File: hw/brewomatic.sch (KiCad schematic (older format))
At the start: 32 parts, among them J1 CON_MAX31865, J10 TEST_MOC, J2 EXP1, J3 EXP2, J4 12V_IN, J5 230V_CONN, J6 HEATING_CONN, J7 PUMP_CONN, J8 12V_ALIM_CONN, J9 TEST_IN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

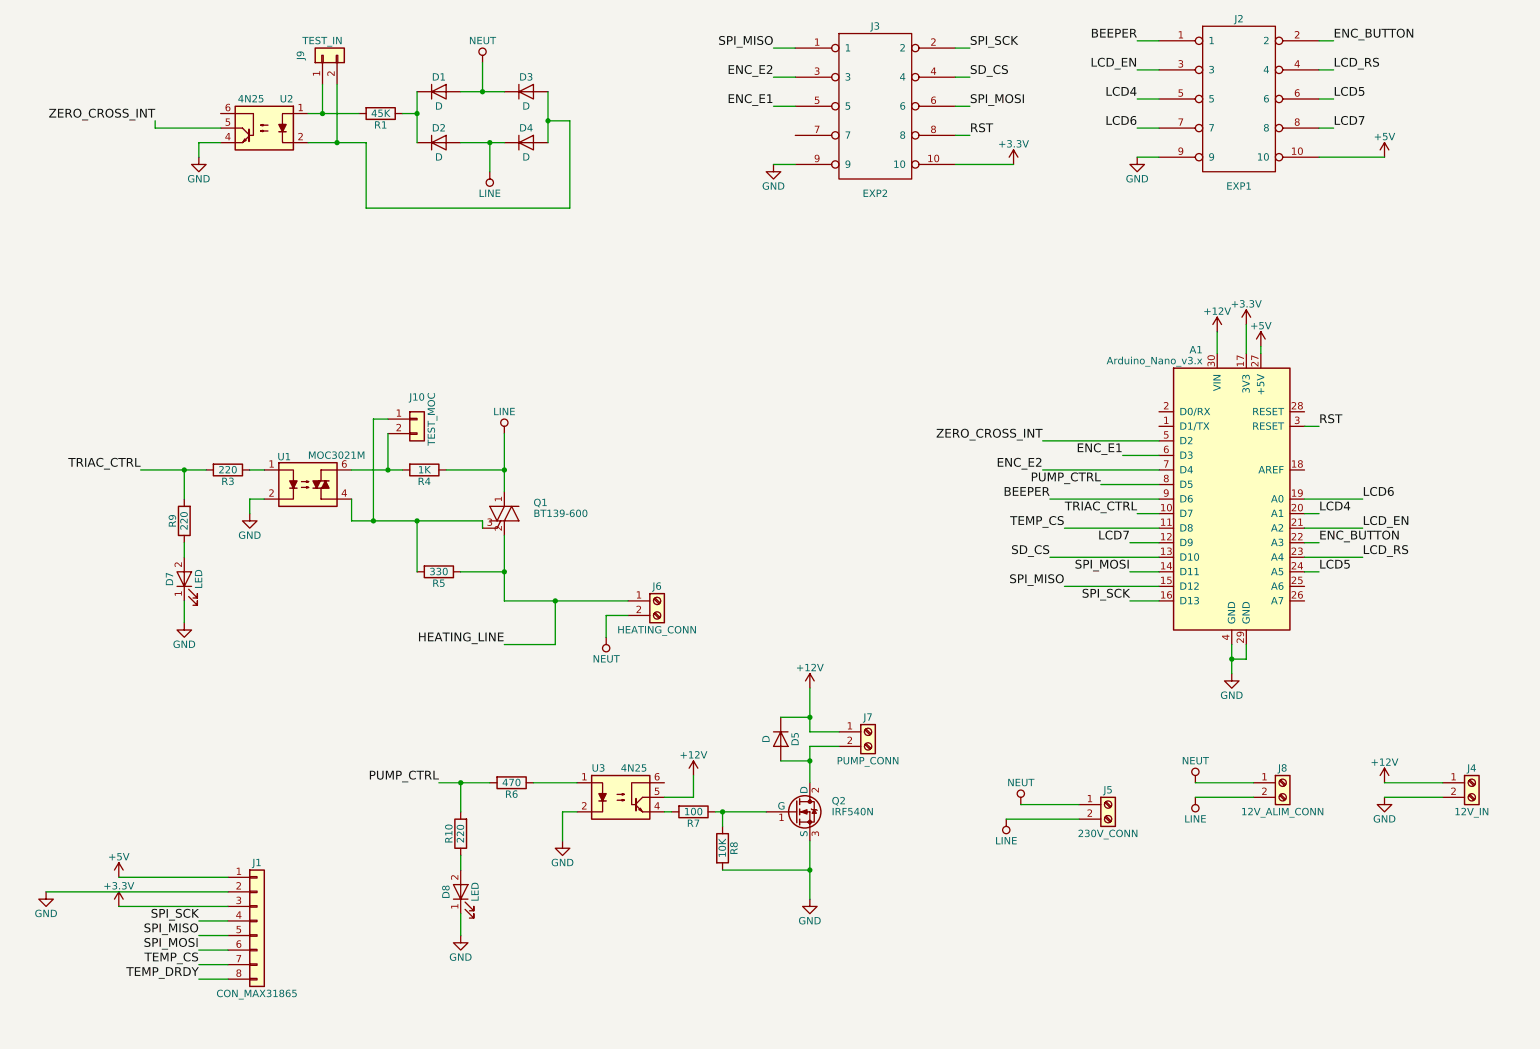
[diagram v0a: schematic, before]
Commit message: Reverse triac terminal since it only works in one direction and fix various problems
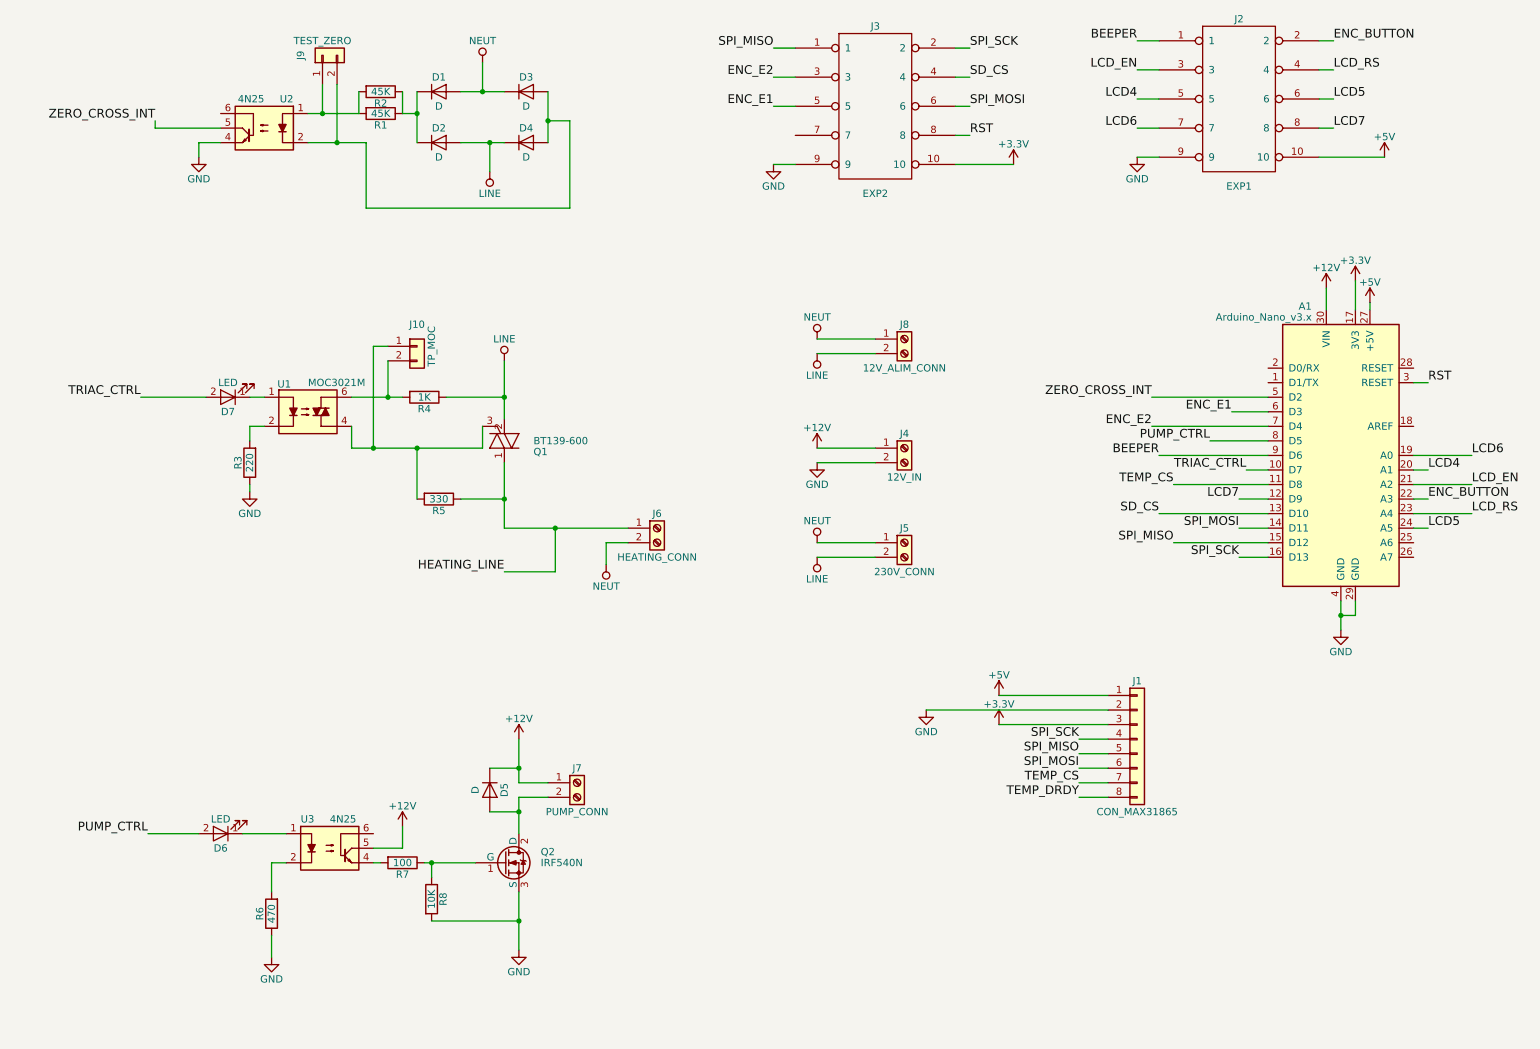
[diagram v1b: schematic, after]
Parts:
- removed D8: LED, LEDs:LED_D5.0mm, symbol LED
- removed R10, R9: 220, Resistors_SMD:R_0805_HandSoldering, symbol R
- added D6: LED, LEDs:LED_D5.0mm, symbol LED
- added R2: 45K, Resistors_THT:R_Axial_DIN0207_L6.3mm_D2.5mm_P10.16mm_Horizontal, symbol R
- J10: value TEST_MOC -> TP_MOC
- J9: value TEST_IN -> TEST_ZERO
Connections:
- net GND: now also R3.1, R6.1; no longer D7.1 (K), U1.2, U3.2
- net HEATING_LINE: now also Q1.1 (A1); no longer Q1.2 (A2)
- net LINE: now also Q1.2 (A2); no longer Q1.1 (A1)
- net PUMP_CTRL: now also D6.2 (A); no longer R6.2
- net TRIAC_CTRL: now also D7.2 (A); no longer R3.2
- net at J9.1 (Pin_1), R1.2, U2.1: now also R2.2
- net at U1.1: now also D7.1 (K); no longer R3.1
- net at D1.1 (K), D2.1 (K), R1.1: now also R2.1
- net at U3.1: now also D6.1 (K); no longer R6.1
- new net: R3.2, U1.2
- new net: R6.2, U3.2
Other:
- moved on the sheet: A1, D5, D7, J1, J10, J4, J5, J6, J7, J8, Q1, Q2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

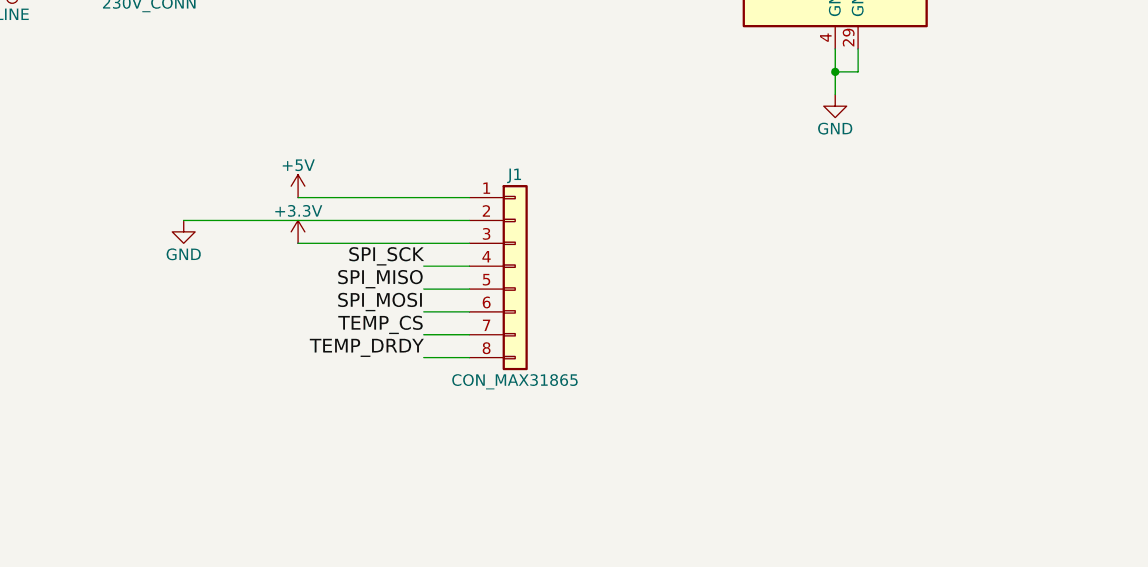
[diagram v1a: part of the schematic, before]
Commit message: Add 12V fan plug
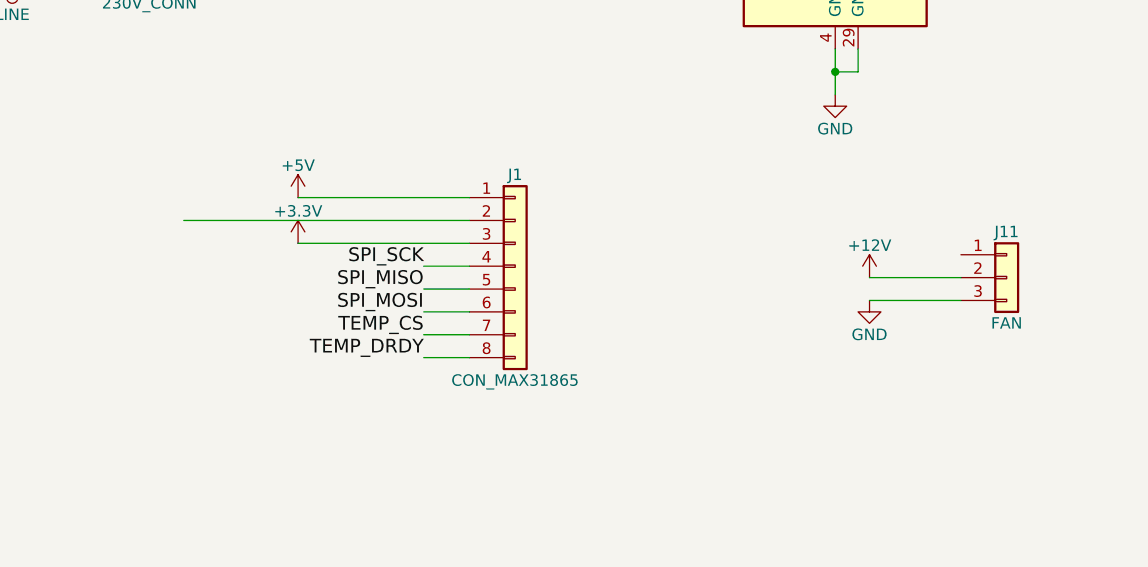
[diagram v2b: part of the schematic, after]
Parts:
- added J11: FAN, Pin_Headers:Pin_Header_Straight_1x03_Pitch2.54mm, symbol Conn_01x03
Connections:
- net +12V: now also J11.2 (Pin_2)
- net GND: now also J11.3 (Pin_3); no longer J1.2 (Pin_2)
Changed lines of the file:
@@
 L GND #PWR010
 U 1 1 5AB865DA
-P 6950 5400
-F 0 "#PWR010" H 6950 5150 50  0001 C CNN
-F 1 "GND" H 6950 5250 50  0000 C CNN
-F 2 "" H 6950 5400 50  0001 C CNN
-F 3 "" H 6950 5400 50  0001 C CNN
-	1    6950 5400
+P 9950 5750
+F 0 "#PWR010" H 9950 5500 50  0001 C CNN
+F 1 "GND" H 9950 5600 50  0000 C CNN
+F 2 "" H 9950 5750 50  0001 C CNN
+F 3 "" H 9950 5750 50  0001 C CNN
+	1    9950 5750
 	1    0    0    -1
 $EndComp
@@
 Wire Wire Line
 	3900 3600 3900 3450
+$Comp
+L Conn_01x03 J11
+U 1 1 5ACBB28D
+P 10550 5650
+F 0 "J11" H 10550 5850 50  0000 C CNN
+F 1 "FAN" H 10550 5450 50  0000 C CNN
+F 2 "Pin_Headers:Pin_Header_Straight_1x03_Pitch2.54mm" H 10550 5650 50  0001 C CNN
+F 3 "" H 10550 5650 50  0001 C CNN
+	1    10550 5650
+	1    0    0    -1
+$EndComp
+$Comp
+L +12V #PWR028
+U 1 1 5ACBC64E
+P 9950 5650
+F 0 "#PWR028" H 9950 5500 50  0001 C CNN
+F 1 "+12V" H 9950 5790 50  0000 C CNN
+F 2 "" H 9950 5650 50  0001 C CNN
+F 3 "" H 9950 5650 50  0001 C CNN
+	1    9950 5650
+	1    0    0    -1
+$EndComp
+Wire Wire Line
+	9950 5750 10350 5750
+Wire Wire Line
+	10350 5650 9950 5650
 $EndSCHEMATC

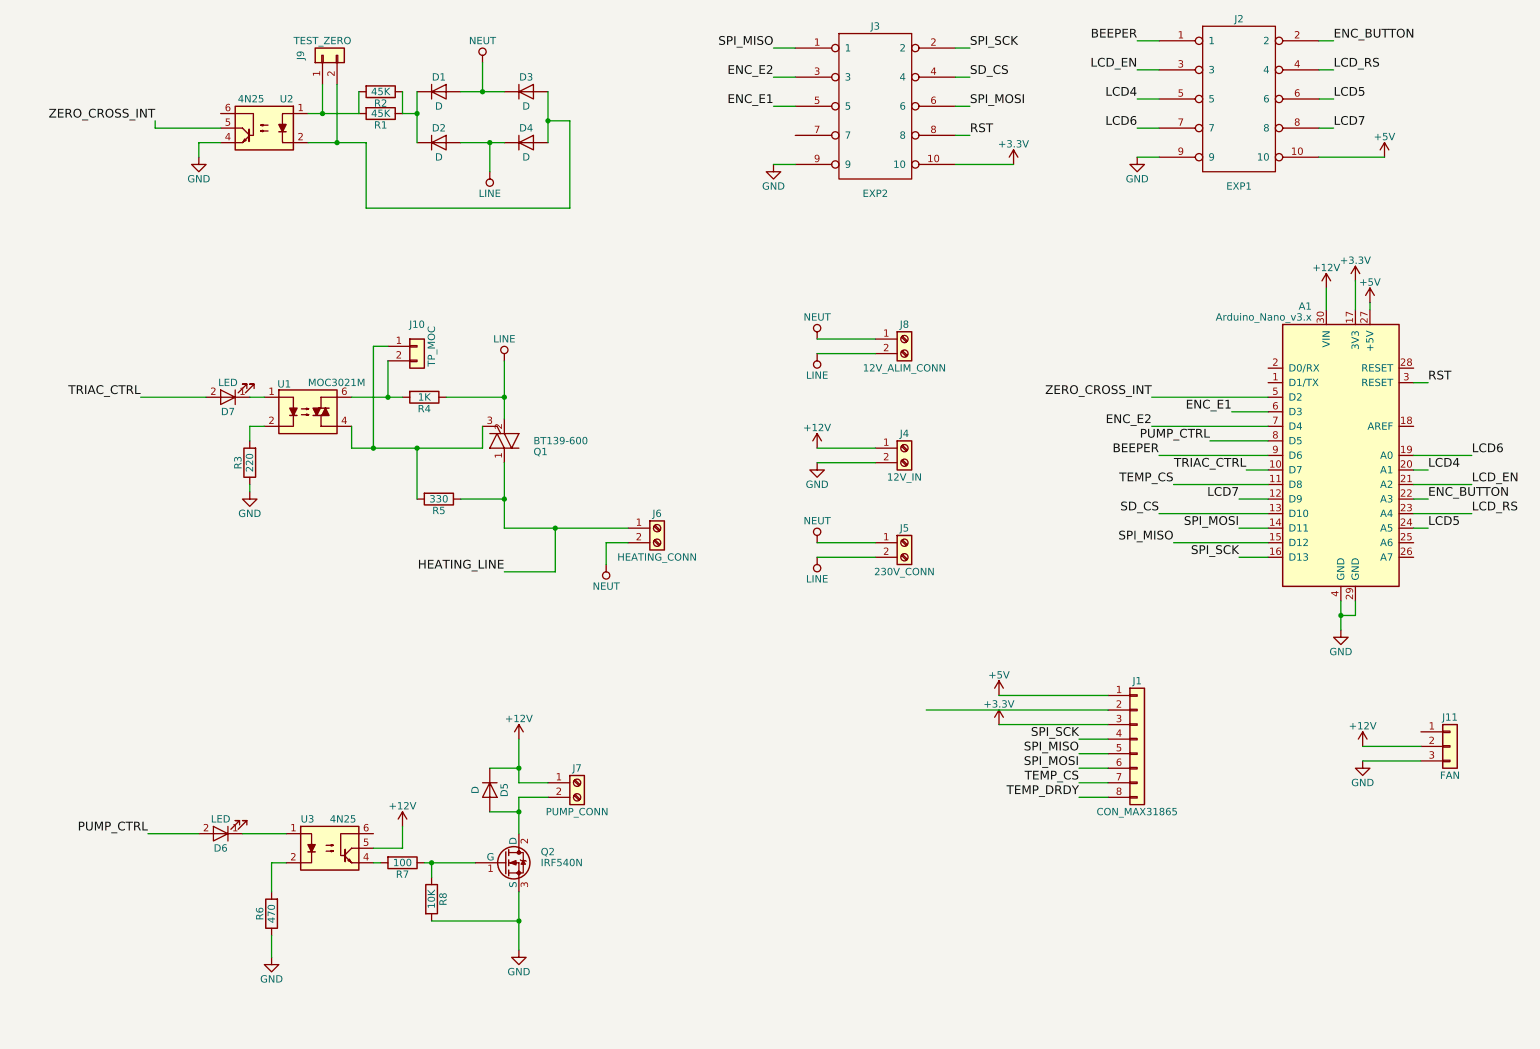
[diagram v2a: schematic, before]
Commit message: HW: Add testpoints on schematic
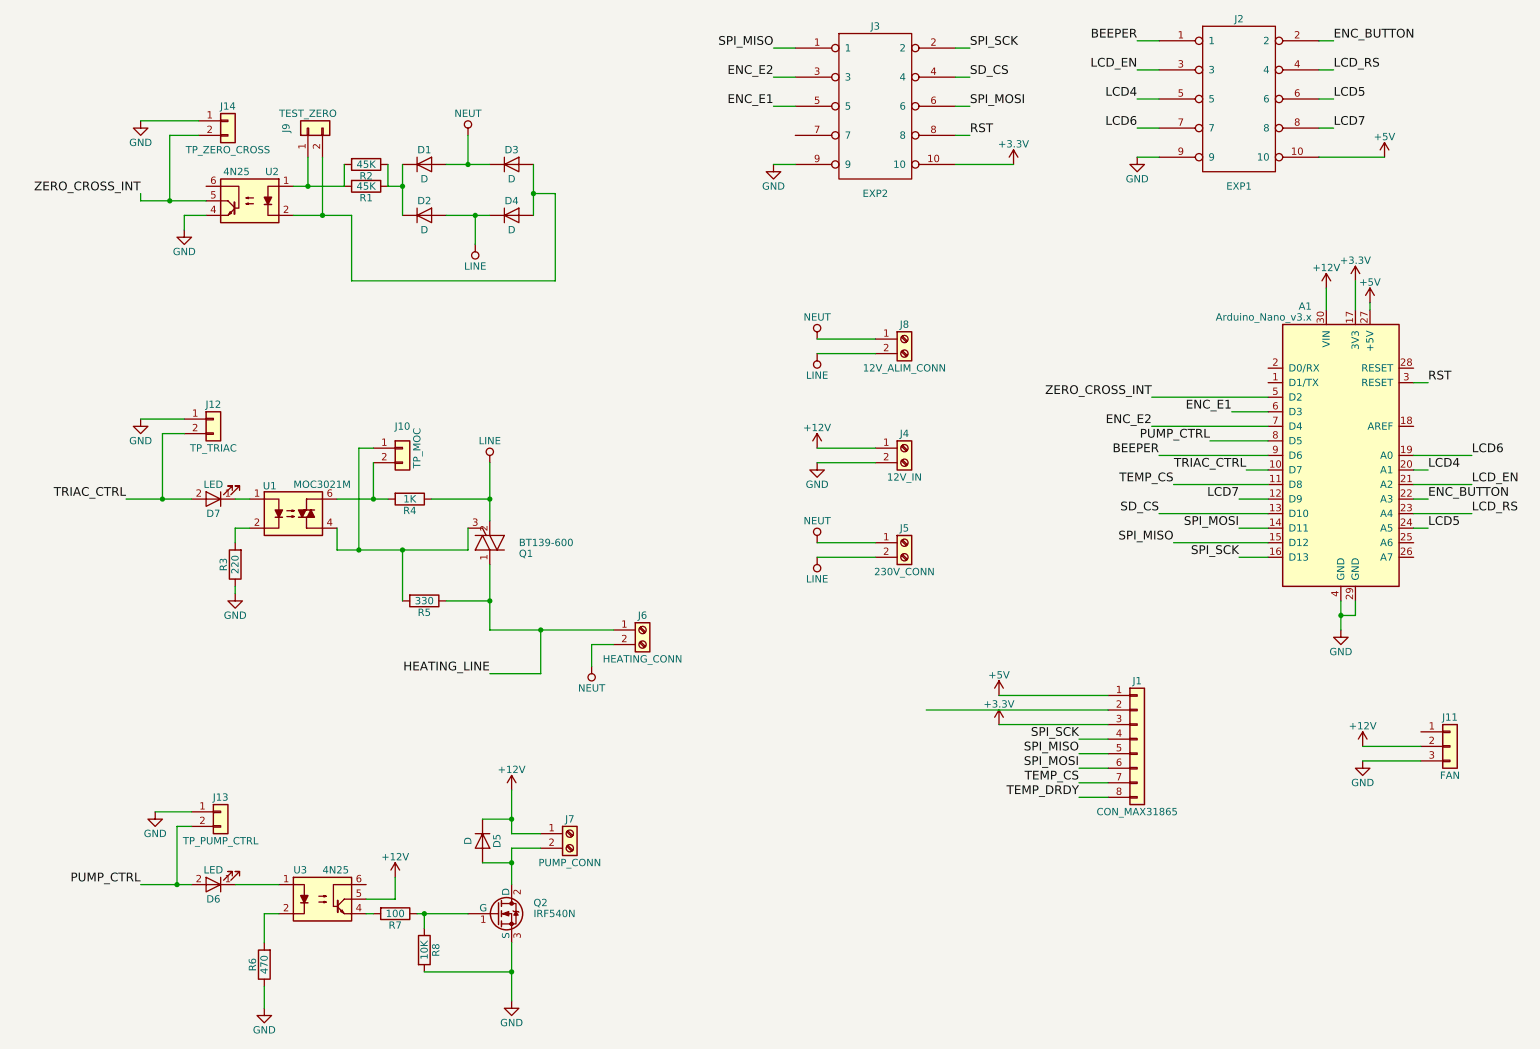
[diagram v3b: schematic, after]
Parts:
- added J12: TP_TRIAC, Pin_Headers:Pin_Header_Straight_1x02_Pitch2.54mm, symbol Conn_01x02
- added J13: TP_PUMP_CTRL, Pin_Headers:Pin_Header_Straight_1x02_Pitch2.54mm, symbol Conn_01x02
- added J14: TP_ZERO_CROSS, Pin_Headers:Pin_Header_Straight_1x02_Pitch2.54mm, symbol Conn_01x02
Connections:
- net GND: now also J12.1 (Pin_1), J13.1 (Pin_1), J14.1 (Pin_1)
- net PUMP_CTRL: now also J13.2 (Pin_2)
- net TRIAC_CTRL: now also J12.2 (Pin_2)
- net ZERO_CROSS_INT: now also J14.2 (Pin_2)
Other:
- moved on the sheet: D1, D2, D3, D4, D5, D6, D7, J10, J6, J7, J9, Q1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

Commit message: hw: Add testpoints for various input/output
This is helpful to plug logic analyzer on them
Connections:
- net GND: now also J1.2 (Pin_2)
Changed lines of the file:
@@
+	1    0    0    -1
+$EndComp
+$Comp
+L GND #PWR?
+U 1 1 5AE4B6BD
+P 6950 5400
+F 0 "#PWR?" H 6950 5150 50  0001 C CNN
+F 1 "GND" H 6950 5250 50  0000 C CNN
+F 2 "" H 6950 5400 50  0001 C CNN
+F 3 "" H 6950 5400 50  0001 C CNN
+	1    6950 5400
 	1    0    0    -1
 $EndComp
